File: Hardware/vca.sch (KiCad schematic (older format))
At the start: 59 parts, among them Q1 MMBFJ177, Q2 MMBFJ177, Q3 MMBFJ177, Q4 MMBFJ177, U6 TL074

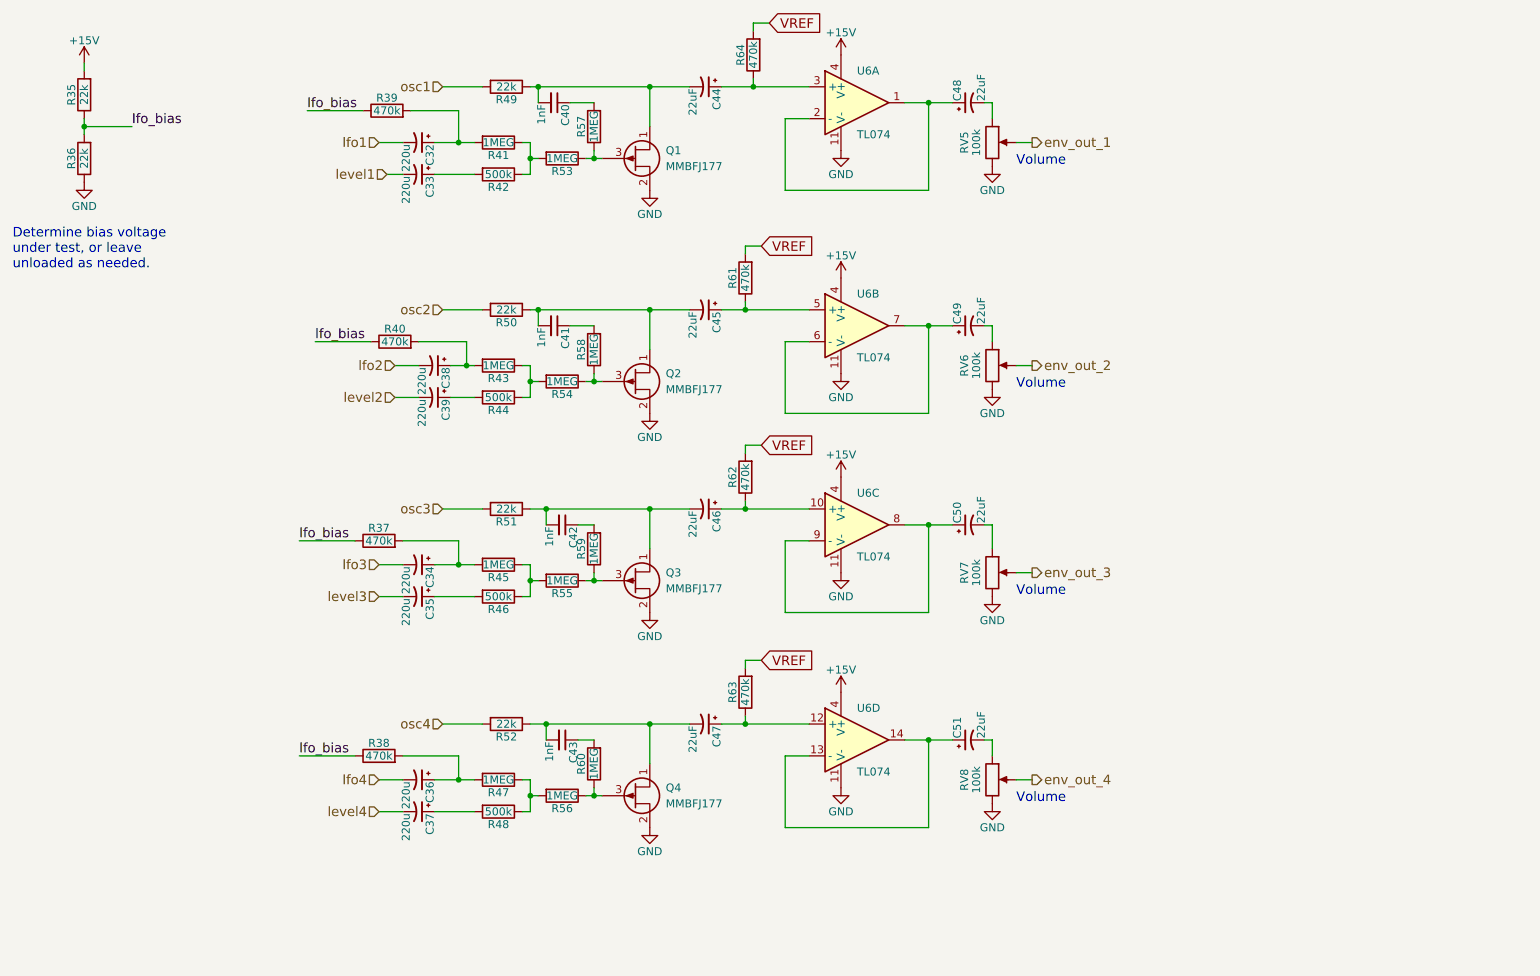
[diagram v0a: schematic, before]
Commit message: change 3.3V to 5V, fix LFO biasing, LPF, JFET bias trim pots.
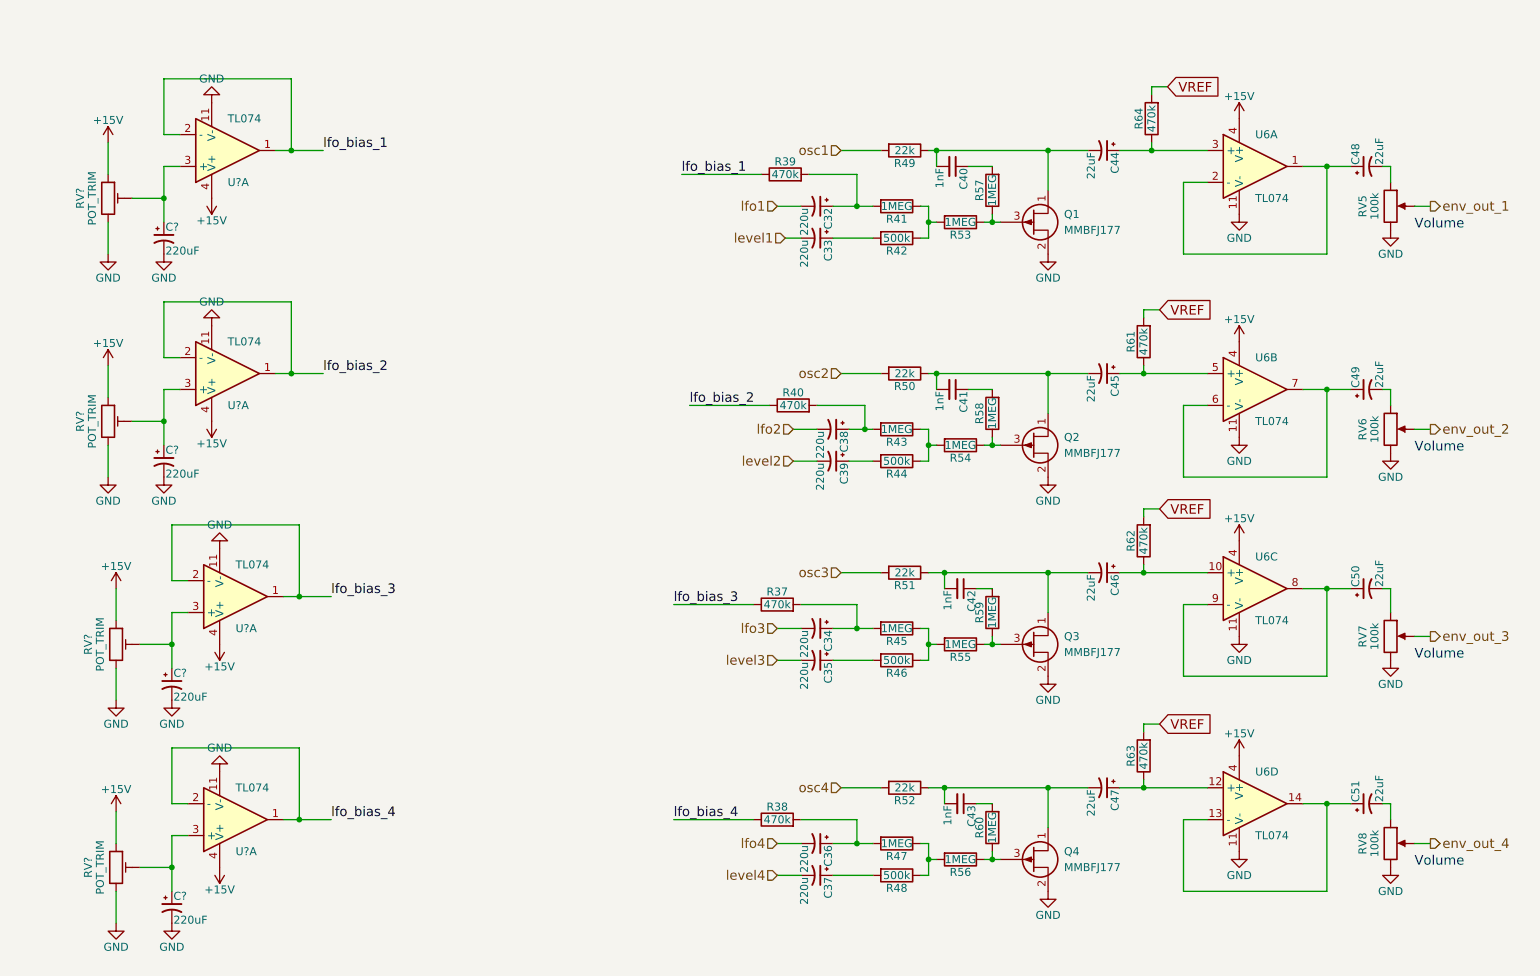
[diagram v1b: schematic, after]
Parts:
- removed R35, R36: 22k, digikey-footprints:0805, symbol R
- added C? (x4): 220uF, Capacitors_SMD:CP_Elec_8x10, symbol CP1_Small
- added RV? (x4): POT_TRIM, symbol POT_TRIM
- added U? (x4): TL074, digikey-footprints:SOIC-14_W3.9mm, symbol TL074
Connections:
- net +15V: now also RV?.1, RV?.1, RV?.1, RV?.1, U?.4 (V+), U?.4 (V+), U?.4 (V+), U?.4 (V+)
- net GND: now also C?.2, C?.2, C?.2, C?.2, RV?.3, RV?.3, RV?.3, RV?.3, U?.11 (V-), U?.11 (V-), U?.11 (V-), U?.11 (V-)
- removed net lfo_bias: R37.1, R38.1, R39.1, R40.1
- new net: C?.1, RV?.2, U?.3 (+) (x4)
- new net lfo_bias_1: R39.1, U?.1, U?.2 (-)
- new net lfo_bias_2: R40.1, U?.1, U?.2 (-)
- new net lfo_bias_3: R37.1, U?.1, U?.2 (-)
- new net lfo_bias_4: R38.1, U?.1, U?.2 (-)
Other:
- note removed: "Determine bias voltage \nunder test, or leave \nunloaded as needed."
- moved on the sheet: C32, C33, C34, C35, C36, C37, C38, C39, C40, C41, C42, C43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

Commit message: add quantization switches
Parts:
- RV5, RV6, RV7, RV8: value 100k -> 100kA
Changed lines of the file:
@@
 P 9200 1700
 F 0 "RV5" V 9025 1700 50  0000 C CNN
-F 1 "100k" V 9100 1700 50  0000 C CNN
+F 1 "100kA" V 9100 1700 50  0000 C CNN
 F 2 "Potentiometers:Potentiometer_Bourns_PTV09A-1_Horizontal" H 9200 1700 50  0001 C CNN
 F 3 "" H 9200 1700 50  0001 C CNN
@@
 P 9200 3100
 F 0 "RV6" V 9025 3100 50  0000 C CNN
-F 1 "100k" V 9100 3100 50  0000 C CNN
+F 1 "100kA" V 9100 3100 50  0000 C CNN
 F 2 "Potentiometers:Potentiometer_Bourns_PTV09A-1_Horizontal" H 9200 3100 50  0001 C CNN
 F 3 "" H 9200 3100 50  0001 C CNN
@@
 P 9200 4400
 F 0 "RV7" V 9025 4400 50  0000 C CNN
-F 1 "100k" V 9100 4400 50  0000 C CNN
+F 1 "100kA" V 9100 4400 50  0000 C CNN
 F 2 "Potentiometers:Potentiometer_Bourns_PTV09A-1_Horizontal" H 9200 4400 50  0001 C CNN
 F 3 "" H 9200 4400 50  0001 C CNN
@@
 P 9200 5700
 F 0 "RV8" V 9025 5700 50  0000 C CNN
-F 1 "100k" V 9100 5700 50  0000 C CNN
+F 1 "100kA" V 9100 5700 50  0000 C CNN
 F 2 "Potentiometers:Potentiometer_Bourns_PTV09A-1_Horizontal" H 9200 5700 50  0001 C CNN
 F 3 "" H 9200 5700 50  0001 C CNN

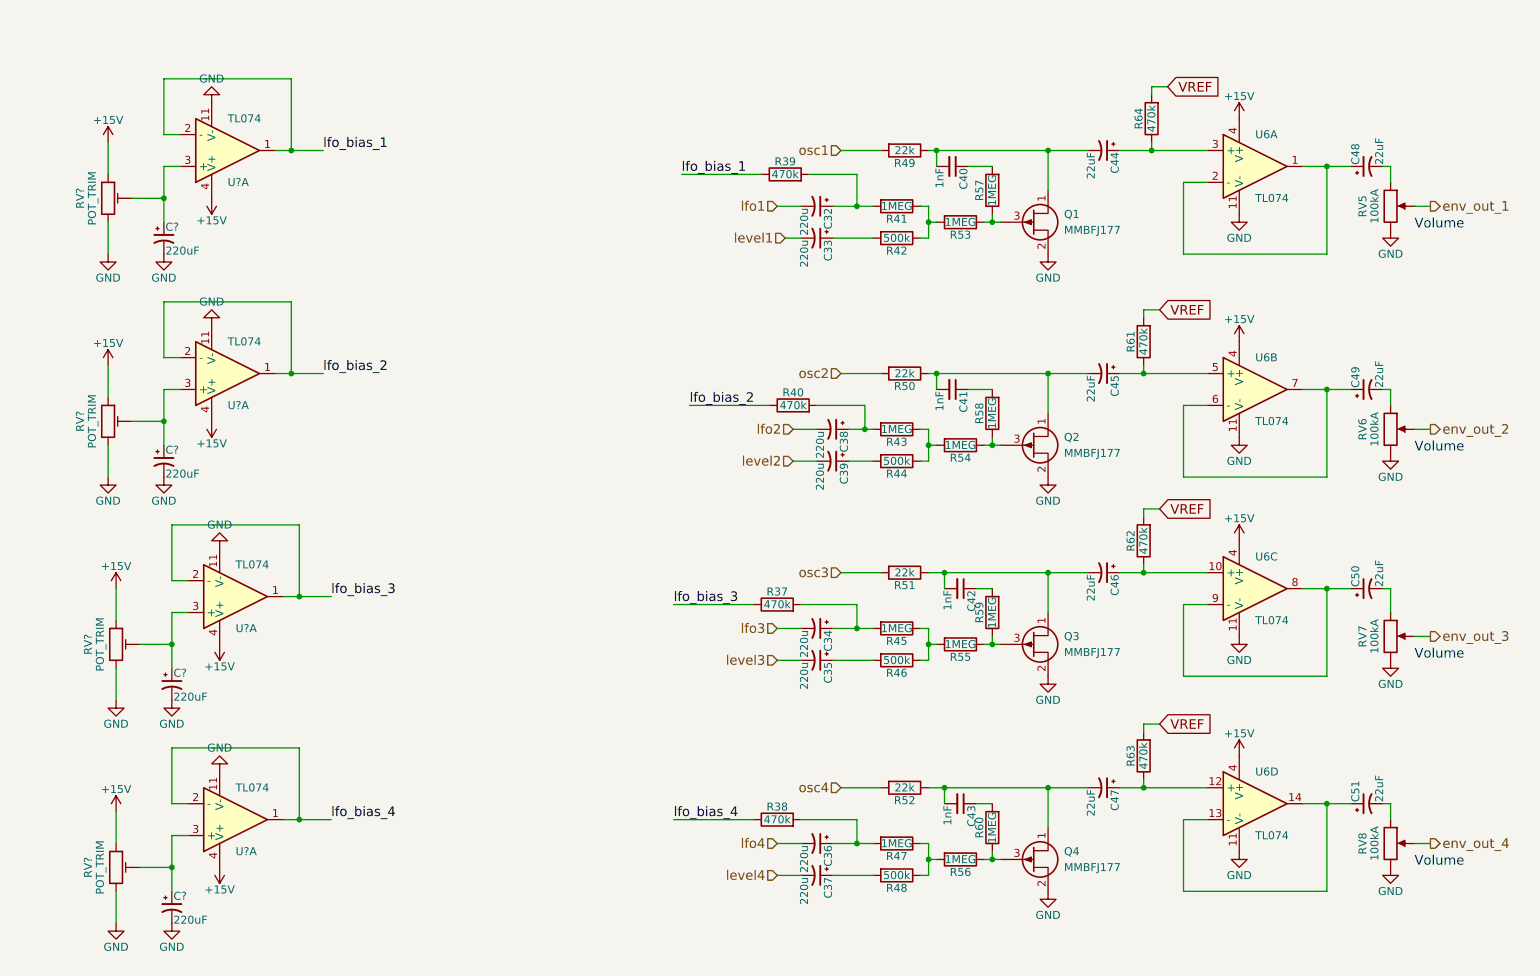
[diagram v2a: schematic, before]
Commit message: update schematics with NPN bias buffer
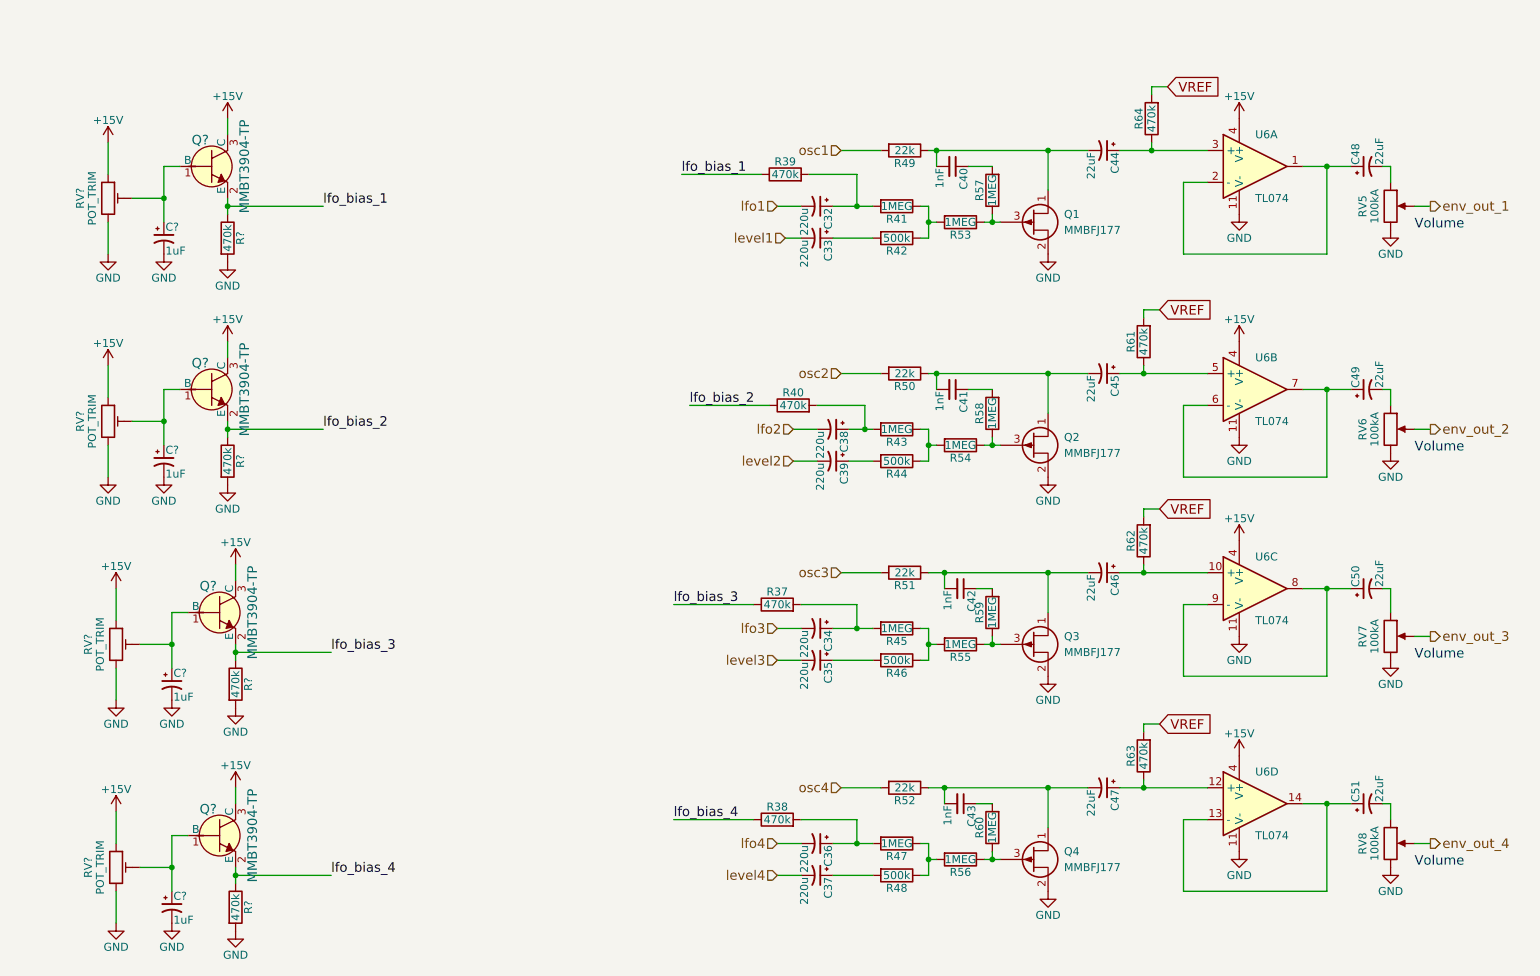
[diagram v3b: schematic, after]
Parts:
- removed U? (x4): TL074, digikey-footprints:SOIC-14_W3.9mm, symbol TL074
- added Q? (x4): MMBT3904-TP, digikey-footprints:SOT-23-3, symbol MMBT3904-TP
- added R? (x4): 470k, digikey-footprints:0805, symbol R
- C? (x4): value 220uF -> 1uF
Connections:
- net +15V: now also Q?.3 (C), Q?.3 (C), Q?.3 (C), Q?.3 (C)
- net GND: now also R?.2, R?.2, R?.2, R?.2
- net lfo_bias_1: now also Q?.2 (E), R?.1
- net lfo_bias_2: now also Q?.2 (E), R?.1
- net lfo_bias_3: now also Q?.2 (E), R?.1
- net lfo_bias_4: now also Q?.2 (E), R?.1
- net at C?.1, RV?.2: now also Q?.1 (B) (x4)

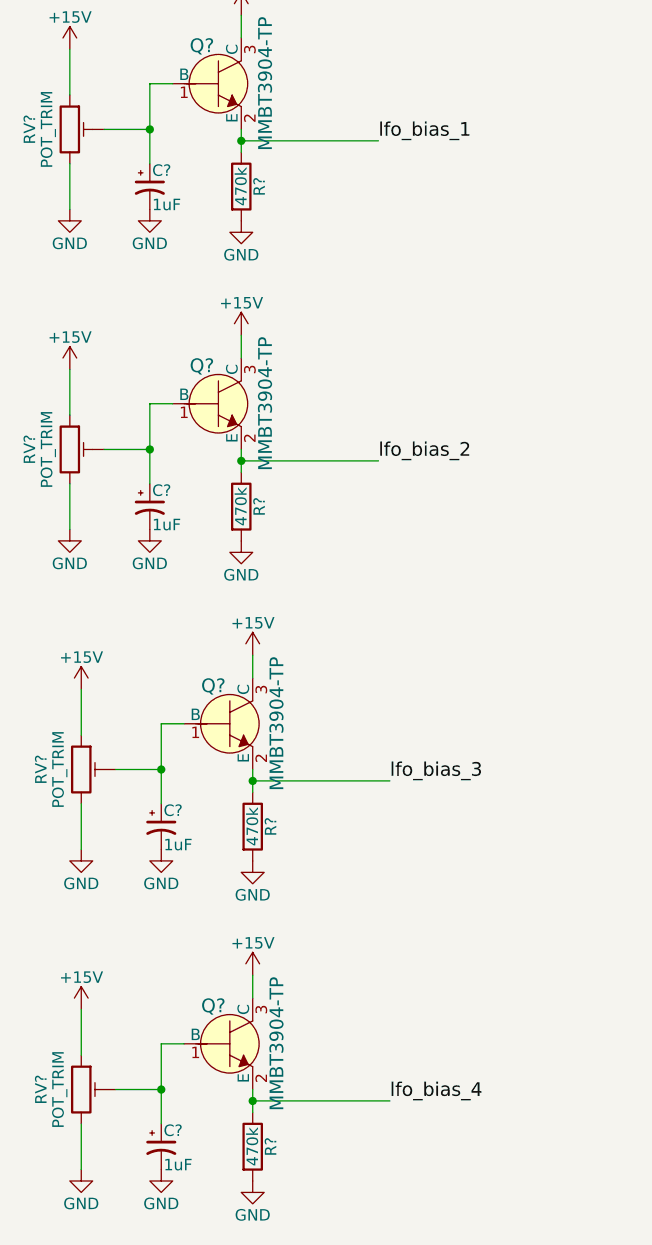
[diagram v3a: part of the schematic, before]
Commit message: change emitter resistors on JFET bias buffers
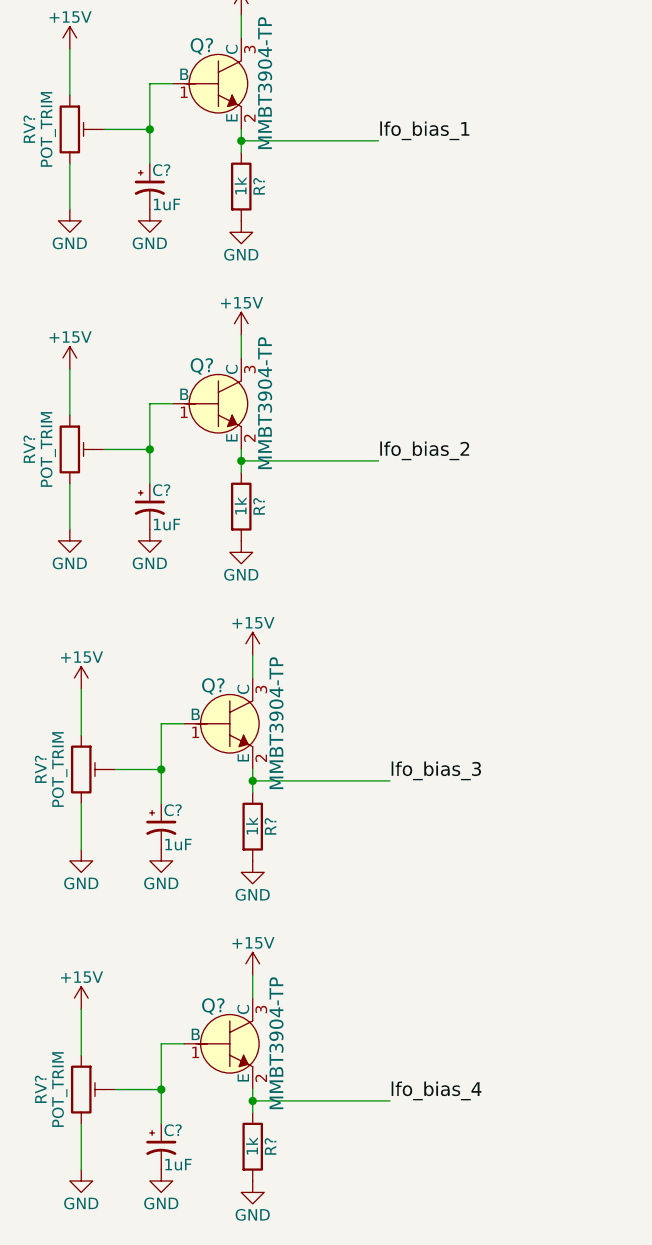
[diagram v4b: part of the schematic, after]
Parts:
- R? (x4): value 470k -> 1k
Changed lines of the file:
@@
 P 1900 1900
 F 0 "R?" V 1980 1900 50  0000 C CNN
-F 1 "470k" V 1900 1900 50  0000 C CNN
+F 1 "1k" V 1900 1900 50  0000 C CNN
 F 2 "digikey-footprints:0805" V 1830 1900 50  0001 C CNN
 F 3 "" H 1900 1900 50  0001 C CNN
@@
 P 1900 3300
 F 0 "R?" V 1980 3300 50  0000 C CNN
-F 1 "470k" V 1900 3300 50  0000 C CNN
+F 1 "1k" V 1900 3300 50  0000 C CNN
 F 2 "digikey-footprints:0805" V 1830 3300 50  0001 C CNN
 F 3 "" H 1900 3300 50  0001 C CNN
@@
 P 1950 4700
 F 0 "R?" V 2030 4700 50  0000 C CNN
-F 1 "470k" V 1950 4700 50  0000 C CNN
+F 1 "1k" V 1950 4700 50  0000 C CNN
 F 2 "digikey-footprints:0805" V 1880 4700 50  0001 C CNN
 F 3 "" H 1950 4700 50  0001 C CNN
@@
 P 1950 6100
 F 0 "R?" V 2030 6100 50  0000 C CNN
-F 1 "470k" V 1950 6100 50  0000 C CNN
+F 1 "1k" V 1950 6100 50  0000 C CNN
 F 2 "digikey-footprints:0805" V 1880 6100 50  0001 C CNN
 F 3 "" H 1950 6100 50  0001 C CNN
